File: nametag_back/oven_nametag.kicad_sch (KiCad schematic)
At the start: 7 parts, among them SW2 SW_SPDT, U1 TPS613221ADBV

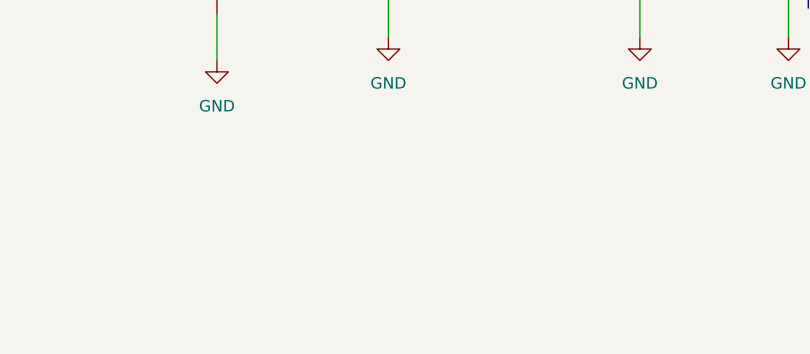
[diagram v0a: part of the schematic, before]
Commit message: Finish both pcbs for a two-tier PCB
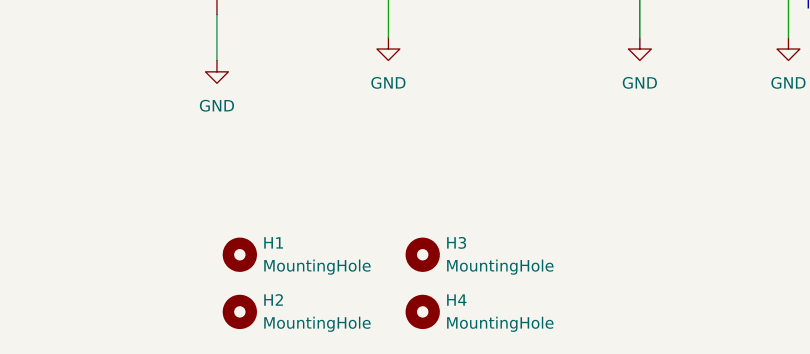
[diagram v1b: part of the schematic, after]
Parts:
- added H1, H2, H3, H4: MountingHole, MountingHole:MountingHole_4.3mm_M4, symbol Mechanical:MountingHole
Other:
- company: (none) -> MAKE Roanoke
- title: (none) -> Two-tier nametag - back

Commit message: Push new fab files
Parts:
- H1, H2, H3, H4: footprint MountingHole:MountingHole_4.3mm_M4 -> MountingHole:MountingHole_3.2mm_M3
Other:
- note added: "Backlight LEDs"
- note added: "Boost Converter"
- note added: "Key Requirements: - approx 3"x4" dimensions - AAA-powered - Boost converter - Power switch"
- note added: "Mechanical"
- note removed: "Key Requirements: - approx 3"x4" dimensions - AAA-powered? (x1 or x2?) - Boost converter - Power switch - Optional: esp add-on"
- company: MAKE Roanoke -> Stan Okrasinski
- moved on the sheet: BT1, C1, C2, H1, H2, H3, H4, L1, RV1, SW2, U1
